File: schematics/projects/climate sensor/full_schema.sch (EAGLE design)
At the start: 49 parts, among them Q1 2N3906BU, Q2 2N3906BU, Q3 2N3906BU, Q4 2N3904, Q5 2N3904

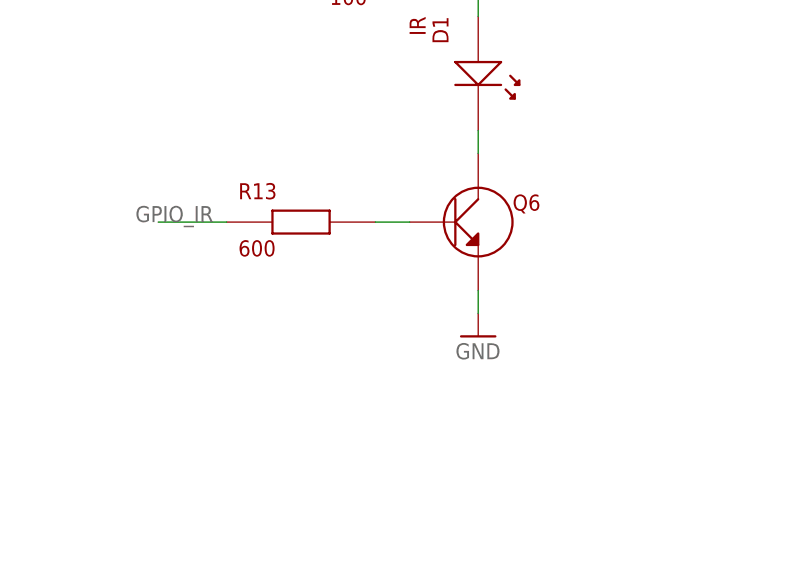
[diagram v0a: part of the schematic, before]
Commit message: Added and tested IR transmitter functionality
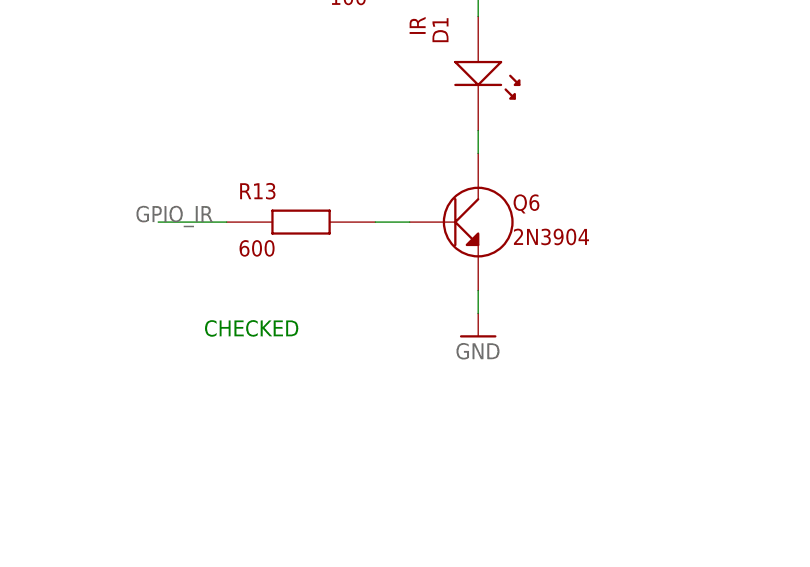
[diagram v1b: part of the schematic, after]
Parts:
- Q6: value (none) -> 2N3904
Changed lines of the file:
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@@
 <part name="D1" library="my_devices" deviceset="LD" device="" value="IR"/>
 <part name="GND10" library="supply1" library_urn="urn:adsk.eagle:library:371" deviceset="GND" device=""/>
-<part name="Q6" library="my_devices" deviceset="TRANSISTOR_NPN" device=""/>
+<part name="Q6" library="my_devices" deviceset="TRANSISTOR_NPN" device="" value="2N3904"/>
 <part name="R12" library="my_devices" deviceset="R" device="" value="100"/>
 <part name="R13" library="my_devices" deviceset="R" device="" value="600"/>
@@
 <text x="-243.84" y="-114.3" size="1.778" layer="91" grouprefs="FAN_SWITCH">CHECKED</text>
 <text x="-391.16" y="68.58" size="1.778" layer="91" grouprefs="ANEMOMETER">CHECKED</text>
+<text x="142.24" y="-83.82" size="1.778" layer="91" grouprefs="IR">CHECKED</text>
 </plain>
 <instances>

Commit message: Prepare library and schematics to create board
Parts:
- removed C3: 10mF, my_devices:C
- removed U$2: TEMP-HUM-PRES-BME280, diy-modules:TEMP-HUM-PRES-BME280
- removed U$3: PMS7003, my_devices:PMS7003
- added U1: BME280, my_devices:BME280
- added U2: PMS7003, my_devices:PMS7003
- U$4: value LIGHT-SENSOR-BH1750 -> BH1750; device diy-modules:LIGHT-SENSOR-BH1750 -> my_devices:BH1750
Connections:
- net +5V: now also C1.PIN_PLUS; no longer C1.P$1, C3.P$2, U$3.VIN, U$3.VIN_1
- net 3V3: no longer U$2.VIN, U$4.VCC
- net GND: now also C1.PIN_GND, U1.GND, U2.GND; no longer C1.P$2, C3.P$1, U$2.GND, U$3.GND, U$3.GND_1
- net I2C_SCL: now also U$4.I2C_SCL, U1.SCL; no longer U$2.SCL, U$4.SCL
- net I2C_SDA: now also U$4.I2C_SDA, U1.SDA; no longer U$2.SDA, U$4.SDA
- net N$28: now also U2.SET; no longer U$3.RESET
- net N$8: now also U2.RESET; no longer U$3.SET
- net UART_1_RXD: now also U2.RXD; no longer U$3.TXD
- net UART_1_TXD: now also U2.TXD; no longer U$3.RXD
- net VCC: now also U$4.VCC, U1.VCC, U2.VCC

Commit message: Continue prepare schematics to create board
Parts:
- removed J4_AN_HWFN_OUT_1, J4_AN_HWFN_OUT_2, J4_AN_HWFN_POWER_1, J4_AN_HWFN_POWER_2, J4_AN_LWHW_OUT_1, J4_AN_LWHW_OUT_2, J4_AN_LWHW_POWER_1, J4_AN_LWHW_POWER_2, J4_FS_2: (no value), con-amp:MTA02-100
- added J1, J4: J2, my_devices:J2
- added J10, J7: KF301-5.0, my_devices:J2
- added J11: J4_FS_2, my_devices:J2
- added J5, J6: WAY AMP 4PIN, my_devices:J4
- J2, J3: value (none) -> J2; device con-amp:MTA02-100 -> my_devices:J2
- J4_FS_1, J8, J9: value (none) -> KF301-5.0; device con-amp:MTA02-100 -> my_devices:J2
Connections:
- net +5V: now also J3.PIN_2, J7.PIN_2; no longer J2.1, J4_AN_LWHW_POWER_1.1
- net 220V_OUT_L: now also J1.PIN_1; no longer J8.2
- net 220V_OUT_N: now also J1.PIN_2; no longer J8.1
- net ACDC_OUT_5V: now also J2.PIN_1; no longer J3.2
- net GND: now also J11.PIN_2, J3.PIN_1, J4_FS_1.PIN_2, J6.PIN_4, J7.PIN_1; no longer J2.2, J4_AN_HWFN_POWER_2.1, J4_AN_LWHW_POWER_1.2, J4_FS_1.1, J4_FS_2.1
- net N$10: now also J4_FS_1.PIN_1; no longer J4_FS_1.2
- net N$11: now also J11.PIN_1; no longer J4_FS_2.2
- net N$12: now also J6.PIN_3; no longer J4_AN_HWFN_POWER_2.2
- net N$13: now also J6.PIN_2; no longer J4_AN_HWFN_OUT_2.1
- net N$14: now also J6.PIN_1; no longer J4_AN_HWFN_OUT_2.2
- net N$15: now also J4.PIN_1; no longer J9.2
- net N$16: now also J4.PIN_2; no longer J9.1
- net N$17: now also J5.PIN_1, J9.PIN_2; no longer J4_AN_HWFN_POWER_1.2, J4_AN_LWHW_POWER_2.1
- net N$18: now also J5.PIN_2, J9.PIN_1; no longer J4_AN_HWFN_POWER_1.1, J4_AN_LWHW_POWER_2.2
- net N$19: now also J10.PIN_2, J5.PIN_3; no longer J4_AN_HWFN_OUT_1.2, J4_AN_LWHW_OUT_2.1
- net N$20: now also J10.PIN_1, J5.PIN_4; no longer J4_AN_HWFN_OUT_1.1, J4_AN_LWHW_OUT_2.2
- net N$25: now also D1.PIN_ANODE; no longer D1.P$2
- net N$26: now also D1.PIN_CATHODE; no longer D1.P$1
- net N$4: now also J8.PIN_1; no longer J4_AN_LWHW_OUT_1.2
- net N$5: now also J8.PIN_2; no longer J4_AN_LWHW_OUT_1.1
- net OUT_GND: now also J2.PIN_2; no longer J3.1
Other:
- moved on the sheet: U$7

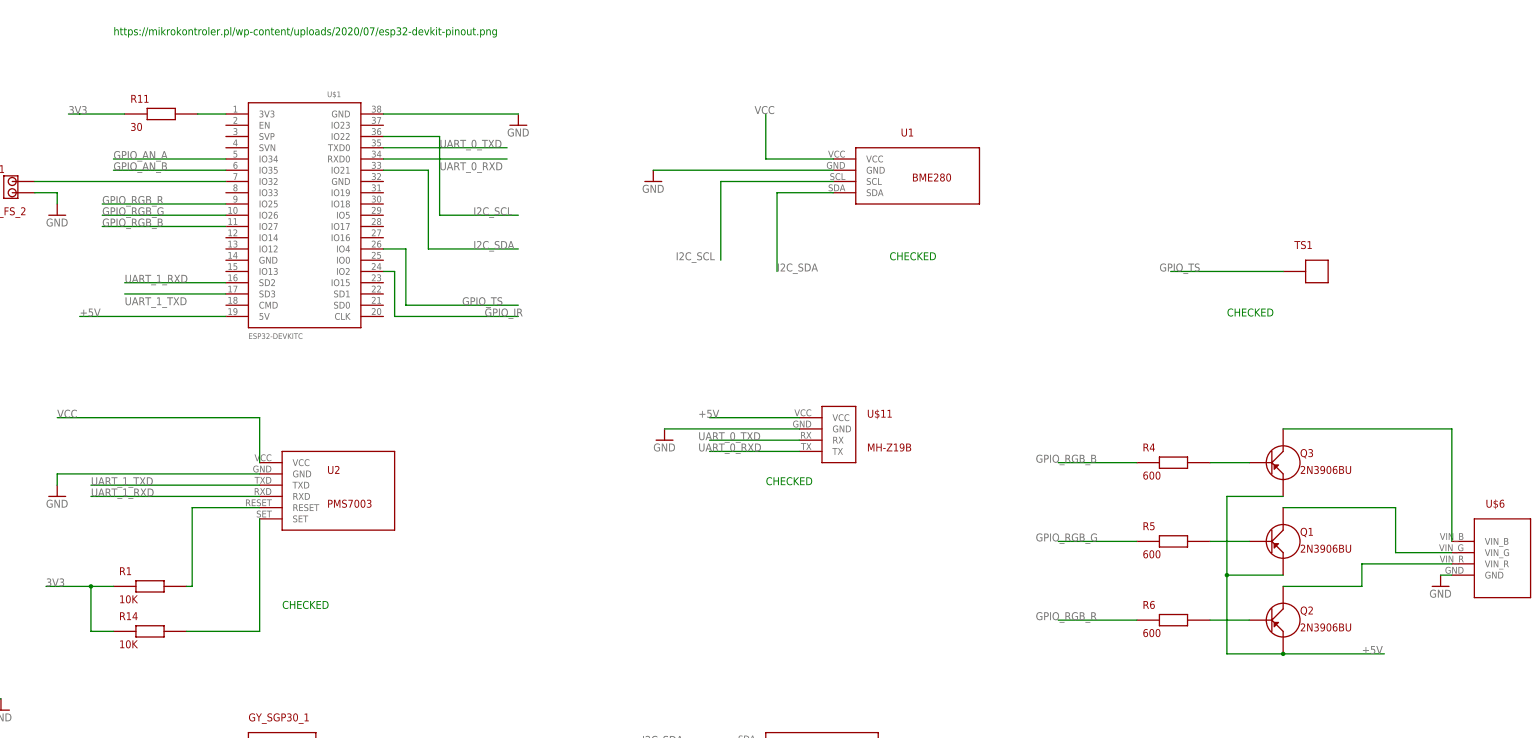
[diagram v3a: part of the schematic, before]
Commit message: rgbled checked and works
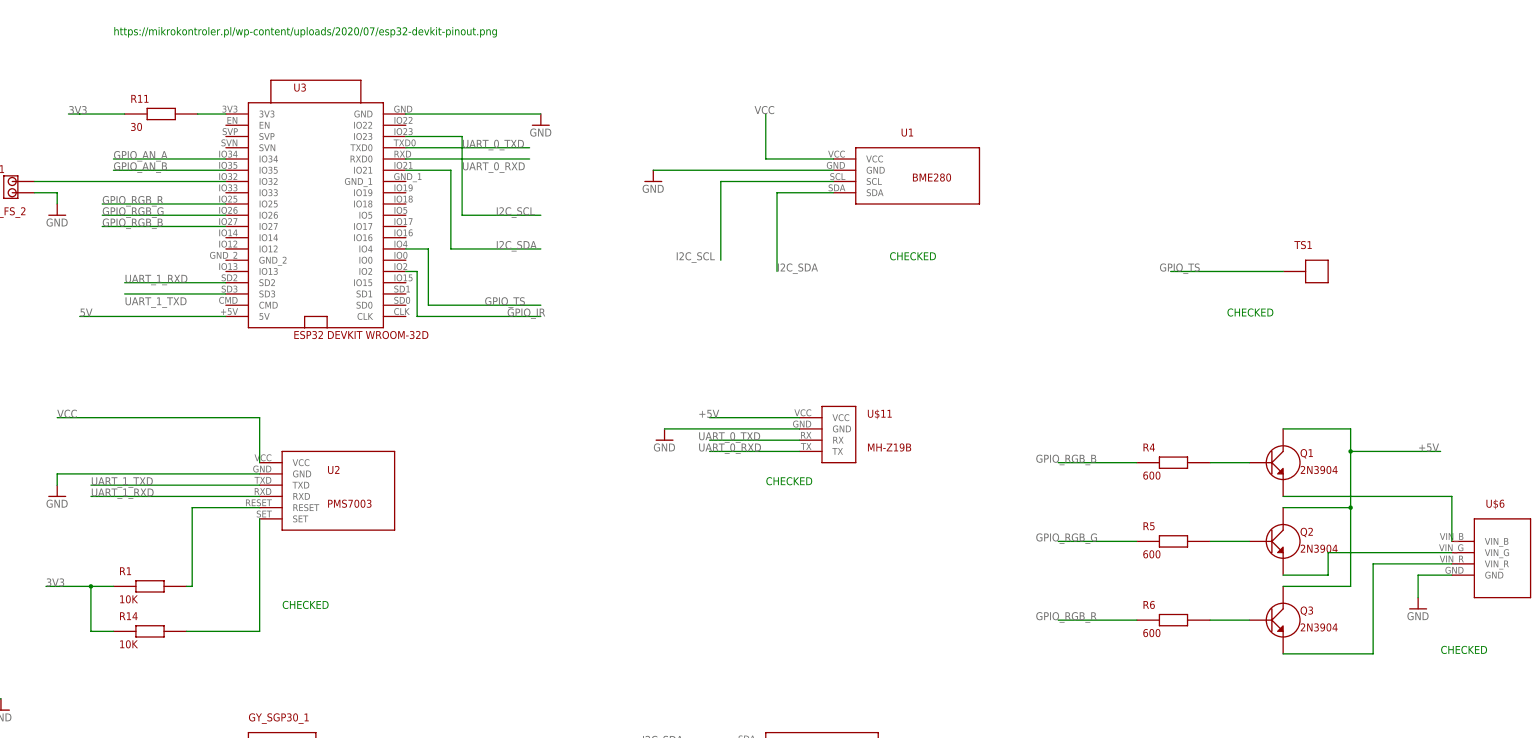
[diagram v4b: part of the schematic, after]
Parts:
- removed U$1: ESP32DEVKITC, ESP32-DEVKITC:ESP32DEVKITC
- added U3: ESP32 DEVKIT WROOM-32D, my_devices:ESP32
- Q1, Q2, Q3: value 2N3906BU -> 2N3904; device my_devices:TRANSISTOR_PNP -> my_devices:TRANSISTOR_NPN
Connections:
- new net 5V: U3.5V
- net +5V: now also Q1.C, Q2.C, Q3.C; no longer Q1.E, Q2.E, Q3.E, U$1.5V
- net GND: now also U3.GND; no longer U$1.GND@38
- net GPIO_AN_A: now also U3.IO34; no longer U$1.IO34
- net GPIO_AN_B: now also U3.IO35; no longer U$1.IO35
- net GPIO_IR: now also U3.IO2; no longer U$1.IO2
- net GPIO_RGB_B: now also U3.IO27; no longer U$1.IO27
- net GPIO_RGB_G: now also U3.IO26; no longer U$1.IO26
- net GPIO_RGB_R: now also U3.IO25; no longer U$1.IO25
- net GPIO_TS: now also U3.IO4; no longer U$1.IO4
- net I2C_SCL: now also U3.IO23; no longer U$1.IO22
- net I2C_SDA: now also U3.IO21; no longer U$1.IO21
- net N$1: now also Q1.E; no longer Q3.C
- net N$11: now also U3.IO32; no longer U$1.IO32
- net N$2: now also Q2.E; no longer Q1.C
- net N$21: now also Q1.B; no longer Q3.B
- net N$22: now also Q2.B; no longer Q1.B
- net N$23: now also Q3.B; no longer Q2.B
- net N$24: now also U3.3V3; no longer U$1.3V3
- net N$3: now also Q3.E; no longer Q2.C
- net UART_0_RXD: now also U3.RXD0; no longer U$1.RXD0
- net UART_0_TXD: now also U3.TXD0; no longer U$1.TXD0
- net UART_1_RXD: now also U3.SD2; no longer U$1.SD2
- net UART_1_TXD: now also U3.SD3; no longer U$1.SD3
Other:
- moved on the sheet: Q1, Q2, Q3
